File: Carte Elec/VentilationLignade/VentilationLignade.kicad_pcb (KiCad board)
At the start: 2 copper layers, 66 parts, among them P1 RelaisBoard1, P10 SDCard, P11 Codeur Rotatif, P12 Teensy Bottom, P13 EndStops1, P14 Teensy_Haut, P15 EndStops2, P16 Teensy_cote, P17 Retour 12V, P18 Masse_12V, P19 12V1, P2 Temp_Ext, P20 12V2, P21 12V_1et2, P22 Teensy_Bas, P23 Serial, P24 Temp_PuitC, P3 RelaisBoard2, P4 Temp_Int, P5 RelaisBoard3, P6 Temp_Chem, P7 RelaisBoard4, P8 RelaisBoard5, P9 TFT, SW1 Reset_Push, SW2 BackLight_On/ff, U2 OPTO-TRANSISTOR, U3 OPTO-TRANSISTOR, U4 OPTO-TRANSISTOR, U5 OPTO-TRANSISTOR, U6 OPTO-TRANSISTOR

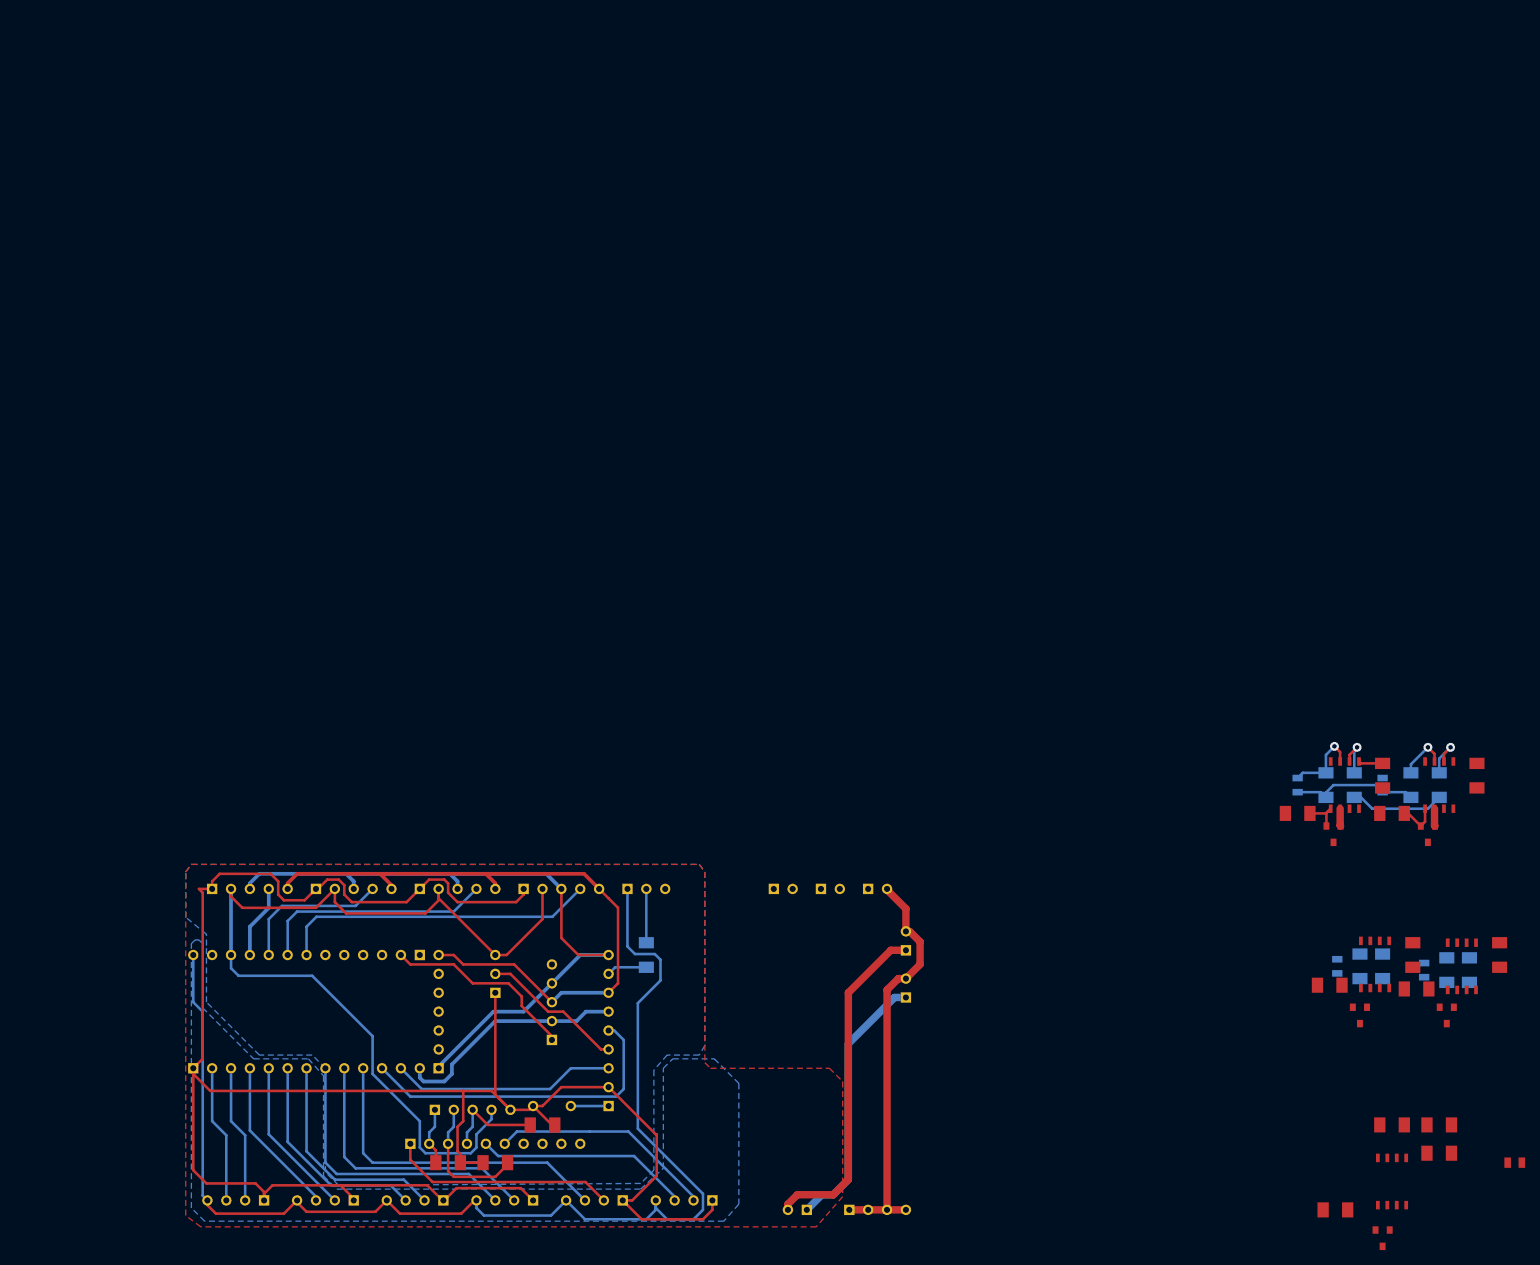
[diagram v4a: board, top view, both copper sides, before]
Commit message: Changement taille 100x160 (pour fab maison)
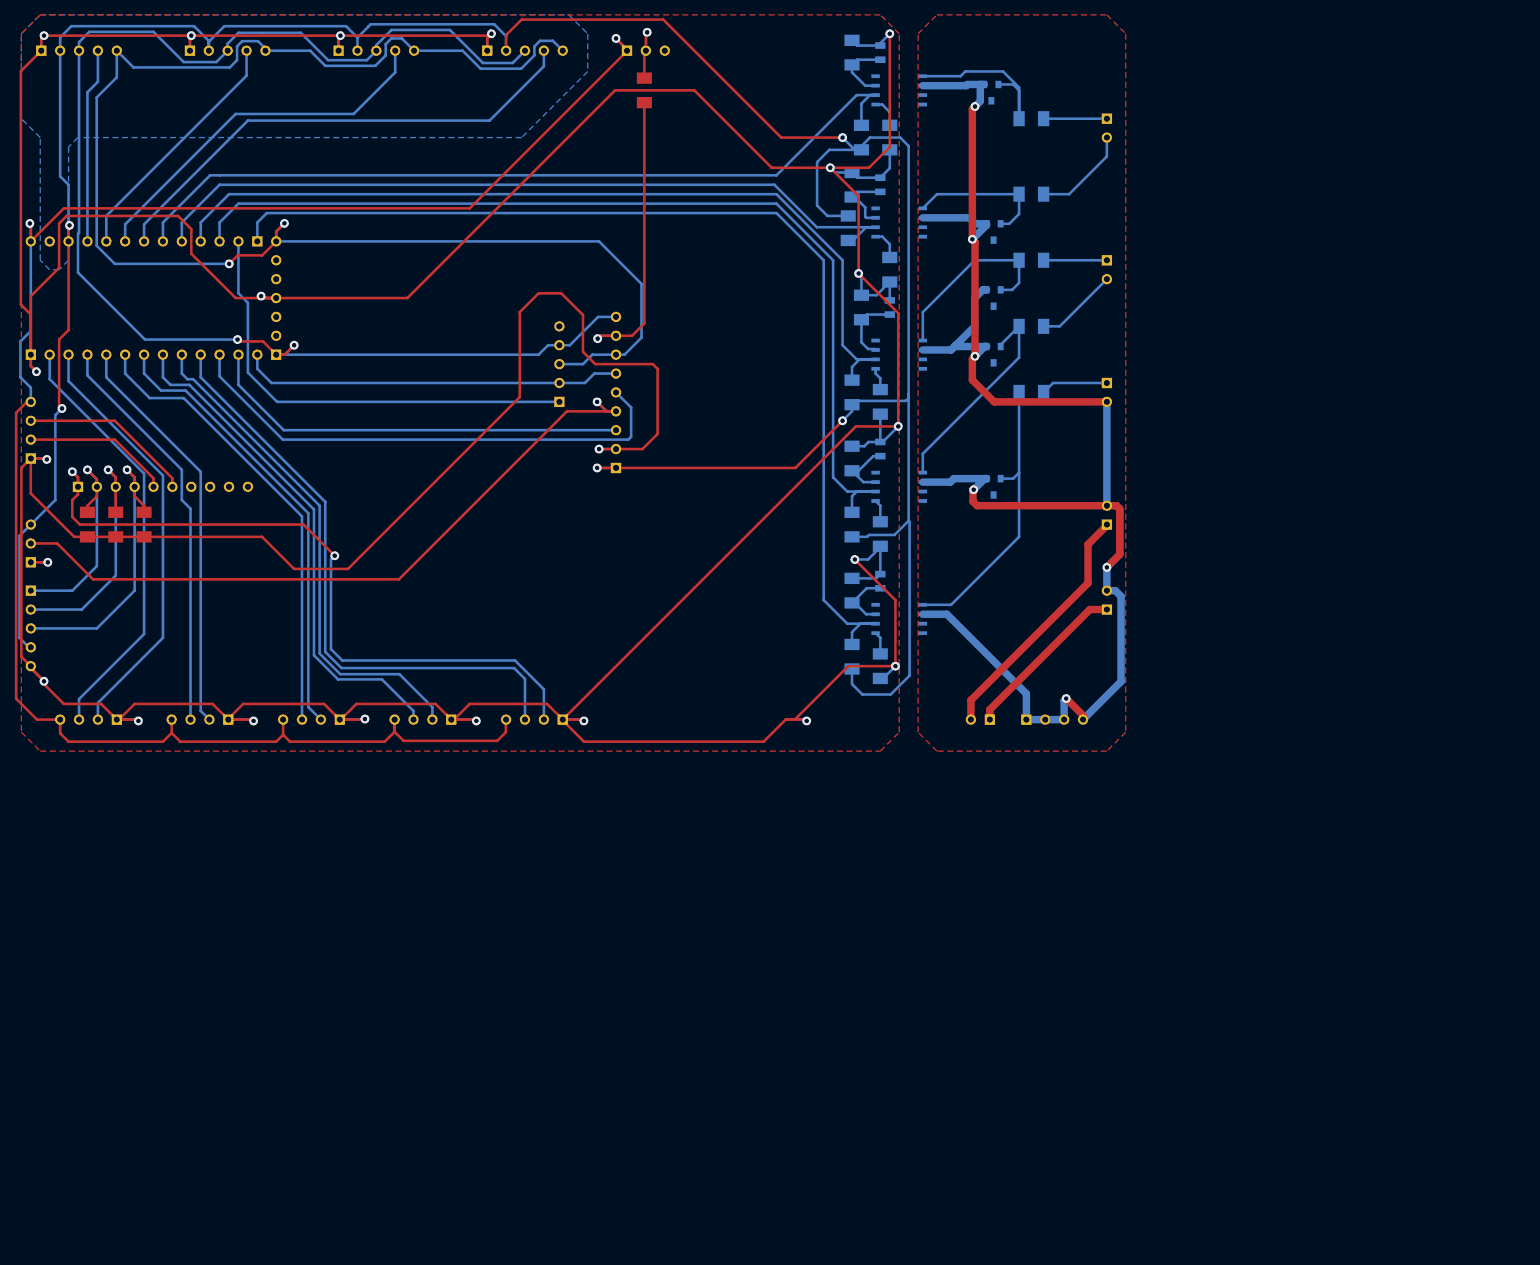
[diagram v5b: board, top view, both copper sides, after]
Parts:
- removed C4: C, C2
- C11, D1, D2, D3, D4, D5, R11, R16, R19, R20, R21, R22, R23, R4, R5, R6, R7, R8, U2, U3, U4, U5, U6: moved to B.Cu
- R1: moved to F.Cu
- moved C11 142.5 mm to (241.0, 141.5), turned to 90 degrees
- moved R9 140.7 mm to (236.0, 107.2), turned to 90 degrees
- moved C9 137.5 mm to (239.8, 107.2), turned to 90 degrees
- moved D3 136.9 mm to (255.0, 140.2), turned to 0 degrees
- moved P23 135.9 mm to (125.5, 158.0), turned to 90 degrees
- moved R11 134.7 mm to (237.2, 141.5), turned to 90 degrees
- moved R6 134.2 mm to (260.1, 135.1), turned to 180 degrees
- moved U2 133.9 mm to (242.3, 112.3), turned to 270 degrees
- moved D1 133.7 mm to (254.7, 112.6), turned to 0 degrees
- moved R10 132.5 mm to (236.0, 125.0), turned to 90 degrees
- moved R14 131.7 mm to (237.2, 118.6)
- moved R19 130.6 mm to (241.0, 118.6)
- moved R15 130.2 mm to (235.4, 130.8), turned to 270 degrees
- moved U4 129.5 mm to (242.3, 147.8), turned to 270 degrees
- moved C10 128.5 mm to (239.8, 125.0), turned to 90 degrees
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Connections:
- P16 pad 4: (no net) -> GND
- P23 pad 2: TX -> RX
- P23 pad 3: RX -> TX
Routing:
- net GND: track 294.7 -> 824.2 mm, vias 0 -> 22
- net +3.3V: track 142.8 -> 385.1 mm, vias 0 -> 5
- net GNDPWR: track 60.1 -> 224.3 mm, vias 0 -> 6
- net 12V_CHECK: track 6.33 -> 141.2 mm, vias 1 -> 0
- net ENDSTOP_2_2: track 5.91 -> 130.6 mm, vias 1 -> 0
- net ENDSTOP_2_1: track 0.00 -> 116.2 mm
- net SPI_SCK: track 90.8 -> 202.8 mm, vias 0 -> 2
- net ENDSTOP_1_1: track 0.00 -> 110.8 mm
- net ENDSTOP_1_2: track 0.00 -> 104.8 mm
- net SPI_MISO: track 92.2 -> 186.6 mm, vias 0 -> 2
- net +5V: track 164.0 -> 245.6 mm, vias 0 -> 2
- net N-0000048: track 19.4 -> 96.2 mm, vias 0 -> 1
- net SELECT_12V: track 30.5 -> 94.3 mm, vias 0 -> 2
- net BYPASS_1_F: track 18.6 -> 58.0 mm
- net BYPASS_1_O: track 18.6 -> 58.0 mm
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- added copper zone on F.Cu, net GNDPWR
- removed copper zone on B.Cu, net +5V

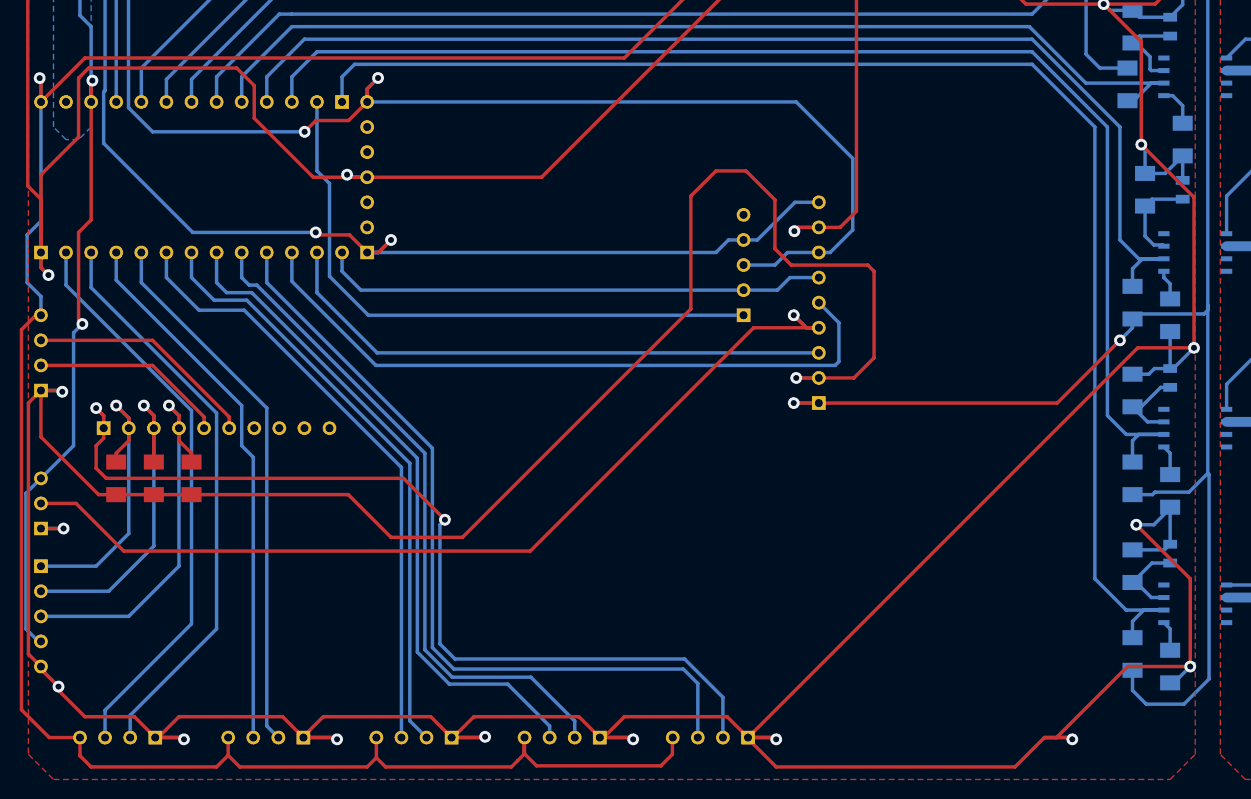
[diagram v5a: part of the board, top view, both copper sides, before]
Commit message: Traceage Poscript
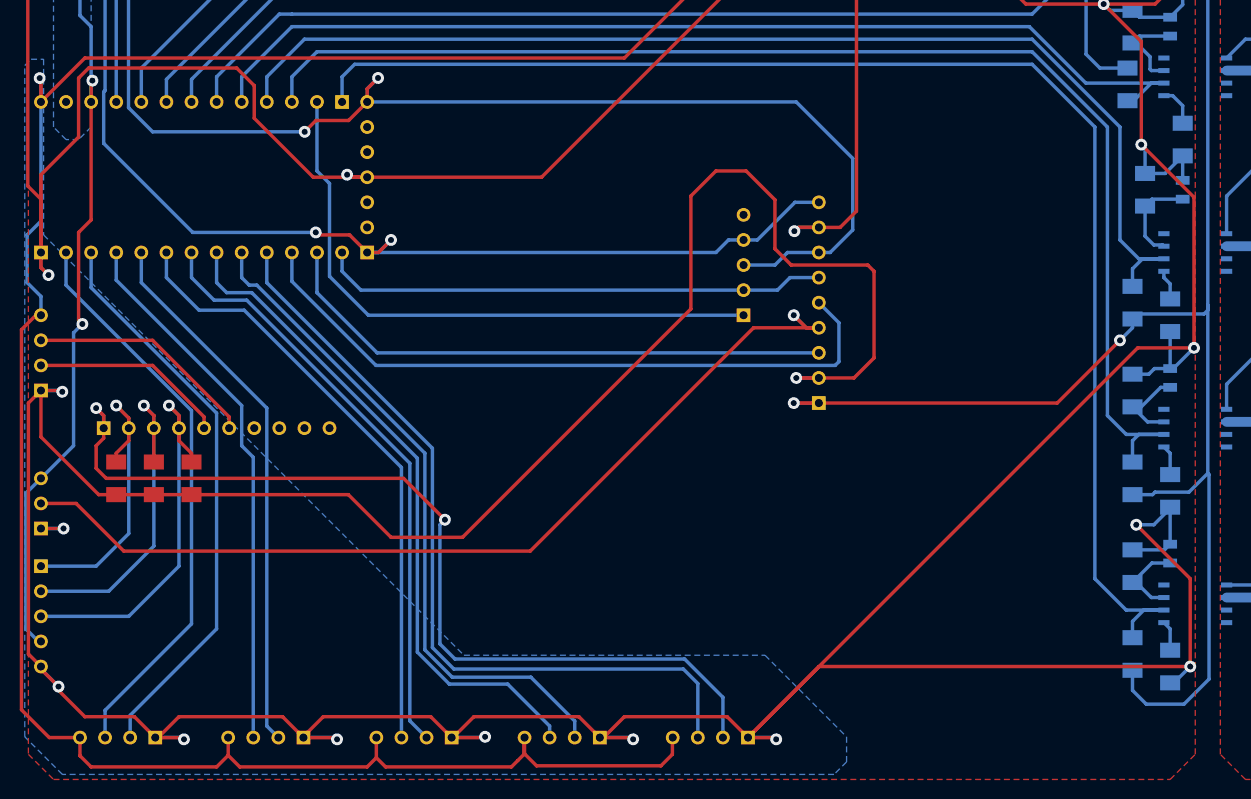
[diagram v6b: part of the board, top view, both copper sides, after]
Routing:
- net GND: track 824.2 -> 815.9 mm, vias 22 -> 21
- added copper zone on B.Cu, net +5V
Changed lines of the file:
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@@
     (area 104.227716 89.078001 274.1964 202.218001)
     (thickness 1.6)
-    (drawings 30)
-    (tracks 773)
+    (drawings 10)
+    (tracks 763)
     (zones 0)
     (modules 65)
@@
     (visible_elements 7FFFFFFF)
     (pcbplotparams
-      (layerselection 3178497)
-      (usegerberextensions true)
+      (layerselection 32769)
+      (usegerberextensions false)
       (excludeedgelayer true)
       (linewidth 0.150000)
@@
       (psnegative false)
       (psa4output false)
-      (plotreference true)
+      (plotreference false)
       (plotvalue true)
       (plotothertext true)
@@
       (padsonsilk false)
       (subtractmaskfromsilk false)
-      (outputformat 1)
+      (outputformat 2)
       (mirror false)
-      (drillshape 1)
+      (drillshape 0)
       (scaleselection 1)
       (outputdirectory ""))
@@
     )
   )
-  (target plus (at 268.972 106.045) (size 0.005) (width 0.1) (layer Contours.Ci))
-  (target plus (at 267.194 107.696) (size 0.005) (width 0.1) (layer Contours.Ci))
-  (target plus (at 269.48 106.045) (size 0.005) (width 0.1) (layer Contours.Ci))
-  (target plus (at 266.686 106.553) (size 0.005) (width 0.1) (layer Contours.Ci))
-  (target plus (at 268.718 107.696) (size 0.005) (width 0.1) (layer Contours.Ci))
-  (target plus (at 268.591 105.283) (size 0.005) (width 0.1) (layer Contours.Ci))
-  (target plus (at 266.94 106.934) (size 0.005) (width 0.1) (layer Contours.Ci))
-  (target plus (at 267.448 106.299) (size 0.005) (width 0.1) (layer Contours.Ci))
-  (target plus (at 268.21 106.045) (size 0.005) (width 0.1) (layer Contours.Ci))
-  (target plus (at 262.749 107.569) (size 0.005) (width 0.1) (layer Contours.Ci))
-  (target plus (at 263.003 108.331) (size 0.005) (width 0.1) (layer Contours.Ci))
-  (target plus (at 263.003 110.363) (size 0.005) (width 0.1) (layer Contours.Ci))
-  (target plus (at 263.257 110.617) (size 0.005) (width 0.1) (layer Contours.Ci))
-  (target plus (at 261.479 112.014) (size 0.005) (width 0.1) (layer Contours.Ci))
-  (target plus (at 259.574 108.458) (size 0.005) (width 0.1) (layer Contours.Ci))
-  (target plus (at 267.194 107.061) (size 0.005) (width 0.1) (layer Contours.Ci))
-  (target plus (at 269.222 104.928) (size 0.005) (width 0.1) (layer Contours.Ci))
-  (target plus (at 272.222 103.928) (size 0.005) (width 0.1) (layer Contours.Ci))
-  (target plus (at 272.222 103.928) (size 0.005) (width 0.1) (layer Contours.Ci))
-  (target plus (at 270.222 104.928) (size 0.005) (width 0.1) (layer Contours.Ci))
-  (target plus (at 269.222 104.928) (size 0.005) (width 0.1) (layer Contours.Ci))
-  (target plus (at 270.222 103.928) (size 0.005) (width 0.1) (layer Contours.Ci))
-  (target plus (at 270.222 104.928) (size 0.005) (width 0.1) (layer Contours.Ci))
-  (target plus (at 269.222 104.928) (size 0.005) (width 0.1) (layer Contours.Ci))
+  (target plus (at 123.825 102.87) (size 0.005) (width 0.1) (layer Contours.Ci))
+  (target plus (at 272.415 102.87) (size 0.005) (width 0.1) (layer Contours.Ci))
+  (target plus (at 272.415 200.66) (size 0.005) (width 0.1) (layer Contours.Ci))
+  (target plus (at 123.825 200.66) (size 0.005) (width 0.1) (layer Contours.Ci))
   (gr_line (start 273.222 201.928) (end 123.222 201.928) (angle 90) (layer Contours.Ci) (width 0.1))
   (gr_line (start 273.222 101.928) (end 273.222 201.928) (angle 90) (layer Contours.Ci) (width 0.1))
@@
   (segment (start 233.412 164.338) (end 233.412 135.128) (width 0.35) (layer Dessous.Cu) (net 23))
   (segment (start 235.317 166.243) (end 233.412 164.338) (width 0.35) (layer Dessous.Cu) (net 23))
+  (segment (start 241.794 189.738) (end 204.222 189.738) (width 0.35) (layer Dessus.Cu) (net 24))
+  (segment (start 204.222 189.738) (end 197.032 196.928) (width 0.35) (layer Dessus.Cu) (net 24))
   (segment (start 158.482 140.208) (end 176.135 140.208) (width 0.35) (layer Dessus.Cu) (net 24))
   (segment (start 225.157 122.682) (end 233.031 122.682) (width 0.35) (layer Dessus.Cu) (net 24))
@@
   (segment (start 127.494 161.798) (end 127.621 161.925) (width 0.35) (layer Dessus.Cu) (net 24))
   (segment (start 182.032 196.928) (end 182.407 196.928) (width 0.35) (layer Dessus.Cu) (net 24))
-  (segment (start 182.407 196.928) (end 184.517 194.818) (width 0.35) (layer Dessus.Cu) (net 24))
-  (segment (start 184.517 194.818) (end 194.922 194.818) (width 0.35) (layer Dessus.Cu) (net 24))
   (segment (start 194.922 194.818) (end 197.032 196.928) (width 0.35) (layer Dessus.Cu) (net 24))
+  (segment (start 184.517 194.818) (end 194.922 194.818) (width 0.35) (layer Dessus.Cu) (net 24))
+  (segment (start 182.407 196.928) (end 184.517 194.818) (width 0.35) (layer Dessus.Cu) (net 24))
   (segment (start 167.032 196.928) (end 167.167 196.928) (width 0.35) (layer Dessus.Cu) (net 24))
   (segment (start 179.922 194.818) (end 182.032 196.928) (width 0.35) (layer Dessus.Cu) (net 24))
@@
   (via (at 139.94 197.104) (size 1.2) (layers Dessus.Cu Dessous.Cu) (net 24))
   (segment (start 139.764 196.928) (end 139.94 197.104) (width 0.35) (layer Dessus.Cu) (net 24))
-  (segment (start 197.032 196.928) (end 197.032 197.046) (width 0.35) (layer Dessus.Cu) (net 24))
-  (segment (start 224.062 199.898) (end 227.032 196.928) (width 0.35) (layer Dessus.Cu) (net 24))
-  (segment (start 199.884 199.898) (end 224.062 199.898) (width 0.35) (layer Dessus.Cu) (net 24))
-  (segment (start 197.032 197.046) (end 199.884 199.898) (width 0.35) (layer Dessus.Cu) (net 24))
-  (segment (start 227.032 196.928) (end 228.254 196.928) (width 0.35) (layer Dessus.Cu) (net 24))
-  (segment (start 235.444 189.738) (end 241.794 189.738) (width 0.35) (layer Dessus.Cu) (net 24))
-  (segment (start 228.254 196.928) (end 235.444 189.738) (width 0.35) (layer Dessus.Cu) (net 24))
-  (segment (start 227.032 196.928) (end 229.68 196.928) (width 0.35) (layer Dessous.Cu) (net 24))
-  (segment (start 229.68 196.928) (end 227.032 196.928) (width 0.35) (layer Dessus.Cu) (net 24))
-  (segment (start 229.856 197.104) (end 229.68 196.928) (width 0.35) (layer Dessus.Cu) (net 24))
-  (via (at 229.856 197.104) (size 1.2) (layers Dessus.Cu Dessous.Cu) (net 24))
-  (segment (start 229.68 196.928) (end 229.856 197.104) (width 0.35) (layer Dessous.Cu) (net 24))
   (segment (start 239.762 173.609) (end 239.762 173.736) (width 0.35) (layer Dessous.Cu) (net 24))
   (segment (start 239.762 173.736) (end 238.111 175.387) (width 0.35) (layer Dessous.Cu) (net 24))
@@
       )
     )
+  )
+  (zone (net 2) (net_name +5V) (layer Dessous.Cu) (hatch edge 0.508)
+    (connect_pads (clearance 0.508))
+    (min_thickness 0.254)
+    (fill (arc_segments 16) (thermal_gap 0.508) (thermal_bridge_width 0.508))
+    (polygon
+      (pts
+        (xy 207.01 199.39) (xy 205.74 200.66) (xy 127.635 200.66) (xy 123.825 196.85) (xy 123.825 128.905)
+        (xy 124.46 128.27) (xy 125.73 128.27) (xy 125.73 146.05) (xy 168.275 188.595) (xy 198.755 188.595)
+        (xy 207.01 196.85)
+      )
+    )
